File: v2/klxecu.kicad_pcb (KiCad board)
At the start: 4 copper layers, 101.6 x 74.9 mm, 71 parts, among them IC1 SP721, J1 cam_sensor, J2 Conn_01x06, J3 DIP8, J4 Conn_02x04_Counter_Clockwise, J5 TACH_OUT, Q1 SSM3K357R, Q2 SSM3K357R, Q3 STP62NS04Z, Q4 SSM3K357R, Q5 SSM3K357R, Q6 SSM3K357R, Q7 SSM3K357R, U1 S36B-WPZK-A, U2 LM2940S-5.0/NOPB, U3 Arduino Mega 2560 Pro, U4 TC4424AVPA

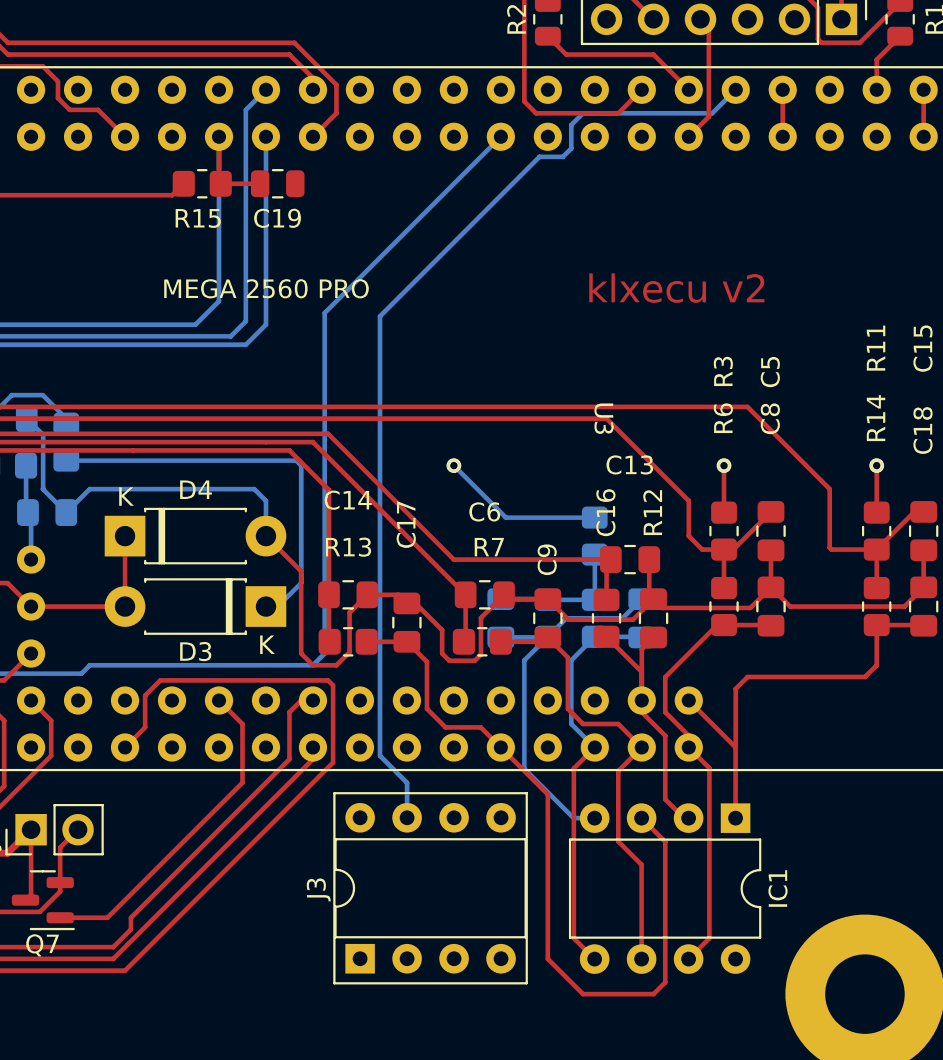
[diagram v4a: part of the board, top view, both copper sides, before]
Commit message: Add reset protection jumper
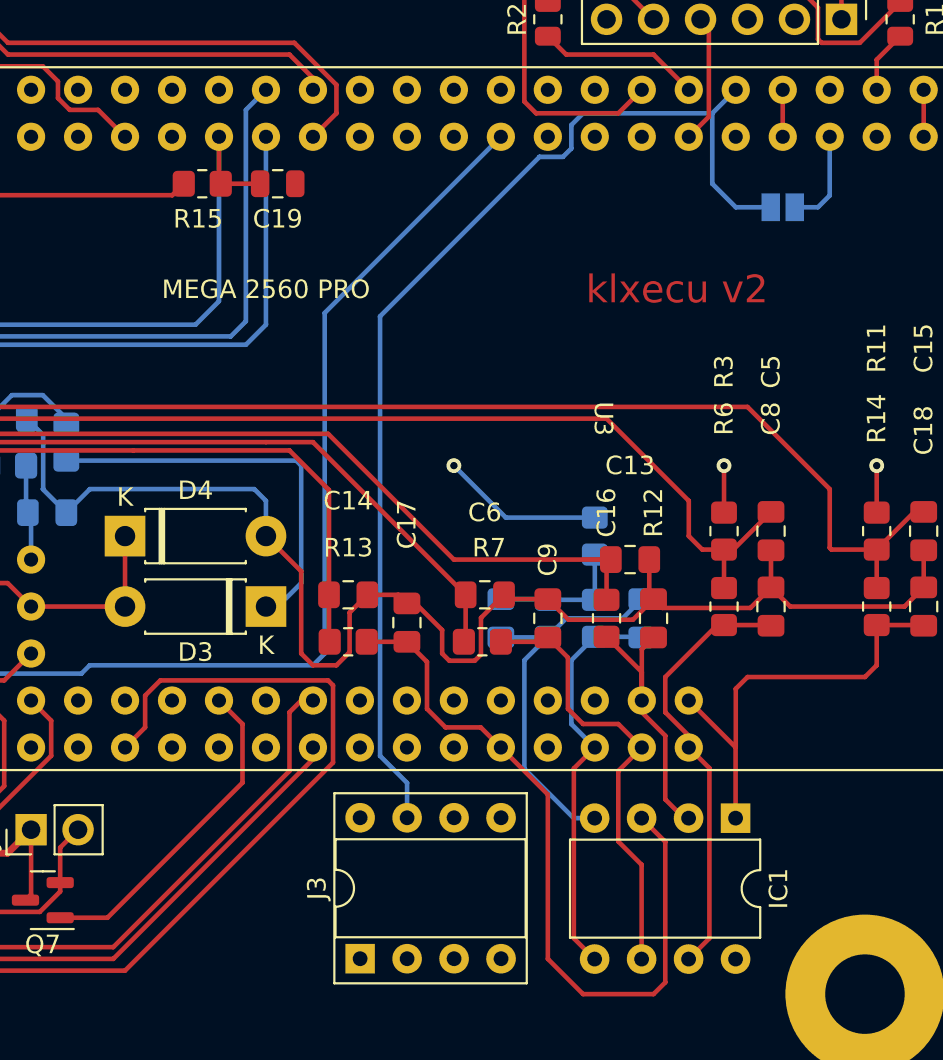
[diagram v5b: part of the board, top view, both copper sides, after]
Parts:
- added JP3: Jumper_2_Open, Jumper:SolderJumper-2_P1.3mm_Open_Pad1.0x1.5mm, B.Cu at (117.5, 66.7)
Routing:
- net ARDUINO-RST: track 52.8 -> 60.3 mm
- net +5V: track 78.0 -> 83.3 mm
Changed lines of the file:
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@@
       (drillshape 0)
       (scaleselection 1)
-      (outputdirectory "gerber/")
+      (outputdirectory "gerber2/")
     )
   )
@@
     (fp_line (start -1 0.625) (end -1 -0.625) (layer "F.Fab") (width 0.1))
     (fp_line (start 1 0.625) (end -1 0.625) (layer "F.Fab") (width 0.1))
-    (pad "1" smd roundrect (at -1.0375 0) (size 1.175 1.45) (layers "F.Cu" "F.Paste" "F.Mask") (roundrect_rratio 0.212766)
+    (pad "1" smd roundrect (at -1.0375 0) (size 1.175 1.45) (layers "F.Cu" "F.Paste" "F.Mask") (roundrect_rratio 0.2127659574)
       (net 119 "O2S") (pintype "passive"))
-    (pad "2" smd roundrect (at 1.0375 0) (size 1.175 1.45) (layers "F.Cu" "F.Paste" "F.Mask") (roundrect_rratio 0.212766)
+    (pad "2" smd roundrect (at 1.0375 0) (size 1.175 1.45) (layers "F.Cu" "F.Paste" "F.Mask") (roundrect_rratio 0.2127659574)
       (net 1 "GND") (pintype "passive"))
     (model "${KICAD6_3DMODEL_DIR}/Capacitor_SMD.3dshapes/C_0805_2012Metric.wrl"
@@
     (fp_line (start -1 0.625) (end -1 -0.625) (layer "F.Fab") (width 0.1))
     (fp_line (start 1 0.625) (end -1 0.625) (layer "F.Fab") (width 0.1))
-    (pad "1" smd roundrect (at -1 0) (size 1.2 1.4) (layers "F.Cu" "F.Paste" "F.Mask") (roundrect_rratio 0.208333)
+    (pad "1" smd roundrect (at -1 0) (size 1.2 1.4) (layers "F.Cu" "F.Paste" "F.Mask") (roundrect_rratio 0.2083333333)
       (net 119 "O2S") (pintype "passive"))
-    (pad "2" smd roundrect (at 1 0) (size 1.2 1.4) (layers "F.Cu" "F.Paste" "F.Mask") (roundrect_rratio 0.208333)
+    (pad "2" smd roundrect (at 1 0) (size 1.2 1.4) (layers "F.Cu" "F.Paste" "F.Mask") (roundrect_rratio 0.2083333333)
       (net 121 "O2S-ARD-A8") (pintype "passive"))
     (model "${KICAD6_3DMODEL_DIR}/Resistor_SMD.3dshapes/R_0805_2012Metric.wrl"
@@
     (fp_line (start -1 -0.625) (end 1 -0.625) (layer "F.Fab") (width 0.1))
     (fp_line (start -1 0.625) (end -1 -0.625) (layer "F.Fab") (width 0.1))
-    (pad "1" smd roundrect (at -1.0375 0 90) (size 1.175 1.45) (layers "F.Cu" "F.Paste" "F.Mask") (roundrect_rratio 0.212766)
+    (pad "1" smd roundrect (at -1.0375 0 90) (size 1.175 1.45) (layers "F.Cu" "F.Paste" "F.Mask") (roundrect_rratio 0.2127659574)
       (net 121 "O2S-ARD-A8") (pintype "passive"))
-    (pad "2" smd roundrect (at 1.0375 0 90) (size 1.175 1.45) (layers "F.Cu" "F.Paste" "F.Mask") (roundrect_rratio 0.212766)
+    (pad "2" smd roundrect (at 1.0375 0 90) (size 1.175 1.45) (layers "F.Cu" "F.Paste" "F.Mask") (roundrect_rratio 0.2127659574)
       (net 1 "GND") (pintype "passive"))
     (model "${KICAD6_3DMODEL_DIR}/Capacitor_SMD.3dshapes/C_0805_2012Metric.wrl"
@@
     )
   )
+  (footprint "Jumper:SolderJumper-2_P1.3mm_Open_Pad1.0x1.5mm" (layer "B.Cu")
+    (at 117.475 66.675 180)
+    (descr "SMD Solder Jumper, 1x1.5mm Pads, 0.3mm gap, open")
+    (tags "solder jumper open")
+    (property "Sheetfile" "sensors.kicad_sch")
+    (property "Sheetname" "Sensors & Inputs")
+    (attr exclude_from_pos_files)
+    (fp_text reference "JP3" (at 0 1.8) (layer "B.SilkS")
+      (effects (font (size 1 1) (thickness 0.15)) (justify mirror))
+    )
+    (fp_text value "Jumper_2_Open" (at 0 -1.9) (layer "B.Fab")
+      (effects (font (size 1 1) (thickness 0.15)) (justify mirror))
+    )
+    (fp_line (start 1.4 1) (end 1.4 -1) (layer "B.SilkS") (width 0.12))
+    (fp_line (start 1.4 -1) (end -1.4 -1) (layer "B.SilkS") (width 0.12))
+    (fp_line (start -1.4 1) (end 1.4 1) (layer "B.SilkS") (width 0.12))
+    (fp_line (start -1.4 -1) (end -1.4 1) (layer "B.SilkS") (width 0.12))
+    (fp_line (start 1.65 -1.25) (end 1.65 1.25) (layer "B.CrtYd") (width 0.05))
+    (fp_line (start -1.65 1.25) (end -1.65 -1.25) (layer "B.CrtYd") (width 0.05))
+    (fp_line (start -1.65 1.25) (end 1.65 1.25) (layer "B.CrtYd") (width 0.05))
+    (fp_line (start 1.65 -1.25) (end -1.65 -1.25) (layer "B.CrtYd") (width 0.05))
+    (pad "1" smd rect (at -0.65 0 180) (size 1 1.5) (layers "B.Cu" "B.Mask")
+      (net 2 "+5V") (pinfunction "A") (pintype "passive"))
+    (pad "2" smd rect (at 0.65 0 180) (size 1 1.5) (layers "B.Cu" "B.Mask")
+      (net 104 "ARDUINO-RST") (pinfunction "B") (pintype "passive"))
+  )
   (footprint "Resistor_SMD:R_0805_2012Metric_Pad1.20x1.40mm_HandSolder" (layer "B.Cu")
     (at 78.74 79.375 90)
@@
   (via (at 114.3 80.645) (size 0.8) (drill 0.4) (layers "F.Cu" "B.Cu") (net 2))
   (via (at 74.93 52.705) (size 0.8) (drill 0.4) (layers "F.Cu" "B.Cu") (free) (net 2))
+  (segment (start 119.38 66.675) (end 118.125 66.675) (width 0.25) (layer "B.Cu") (net 2))
   (segment (start 91.17 80.375) (end 91.44 80.645) (width 0.25) (layer "B.Cu") (net 2))
   (segment (start 46.355 101.8325) (end 46.345 101.8425) (width 1) (layer "B.Cu") (net 2))
+  (segment (start 120.015 62.865) (end 120.015 66.04) (width 0.25) (layer "B.Cu") (net 2))
   (segment (start 90.17 88.265) (end 89.535 88.265) (width 0.25) (layer "B.Cu") (net 2))
   (segment (start 91.44 86.995) (end 90.17 88.265) (width 0.25) (layer "B.Cu") (net 2))
@@
   (segment (start 78.74 80.375) (end 91.17 80.375) (width 0.25) (layer "B.Cu") (net 2))
   (segment (start 91.44 80.645) (end 91.44 86.995) (width 0.25) (layer "B.Cu") (net 2))
+  (segment (start 120.015 66.04) (end 119.38 66.675) (width 0.25) (layer "B.Cu") (net 2))
   (segment (start 62.059511 63.945433) (end 61.415433 64.589511) (width 0.2) (layer "B.Cu") (net 3))
   (segment (start 31.169511 59.259828) (end 32.408859 58.02048) (width 0.2) (layer "B.Cu") (net 3))
@@
   (segment (start 28.845489 91.574511) (end 30.02 90.4) (width 0.25) (layer "In2.Cu") (net 38))
   (segment (start 29.533501 96.574511) (end 28.845489 95.886499) (width 0.25) (layer "In2.Cu") (net 38))
+  (segment (start 81.279282 106.68) (end 90.805 97.154282) (width 0.25) (layer "F.Cu") (net 39))
+  (segment (start 90.805 93.98) (end 91.44 93.345) (width 0.25) (layer "F.Cu") (net 39))
+  (segment (start 90.805 97.154282) (end 90.805 93.98) (width 0.25) (layer "F.Cu") (net 39))
+  (segment (start 91.44 93.345) (end 92.075 93.345) (width 0.25) (layer "F.Cu") (net 39))
   (segment (start 72.0575 105.09) (end 73.6475 106.68) (width 0.25) (layer "F.Cu") (net 39))
-  (segment (start 82.235 105.09) (end 90.805 96.52) (width 0.25) (layer "F.Cu") (net 39))
-  (segment (start 90.805 96.52) (end 90.805 93.98) (width 0.25) (layer "F.Cu") (net 39))
-  (segment (start 81.279282 106.68) (end 82.235 105.724282) (width 0.25) (layer "F.Cu") (net 39))
-  (segment (start 82.235 105.724282) (end 82.235 105.09) (width 0.25) (layer "F.Cu") (net 39))
   (segment (start 73.6475 106.68) (end 81.279282 106.68) (width 0.25) (layer "F.Cu") (net 39))
-  (segment (start 91.44 93.345) (end 92.075 93.345) (width 0.25) (layer "F.Cu") (net 39))
-  (segment (start 90.805 93.98) (end 91.44 93.345) (width 0.25) (layer "F.Cu") (net 39))
   (segment (start 68.58 104.14) (end 70.1825 104.14) (width 0.25) (layer "F.Cu") (net 40))
   (via (at 68.58 104.14) (size 0.8) (drill 0.4) (layers "F.Cu" "B.Cu") (net 40))
@@
   (segment (start 106.045 62.23) (end 106.68 61.595) (width 0.25) (layer "B.Cu") (net 104))
   (segment (start 106.68 61.595) (end 113.665 61.595) (width 0.25) (layer "B.Cu") (net 104))
+  (segment (start 113.665 65.405) (end 114.935 66.675) (width 0.25) (layer "B.Cu") (net 104))
   (segment (start 97.165 99.685) (end 97.165 97.8) (width 0.25) (layer "B.Cu") (net 104))
   (segment (start 95.701511 96.336511) (end 95.701511 72.574207) (width 0.25) (layer "B.Cu") (net 104))
+  (segment (start 114.935 66.675) (end 116.825 66.675) (width 0.25) (layer "B.Cu") (net 104))
+  (segment (start 113.665 61.595) (end 113.665 65.405) (width 0.25) (layer "B.Cu") (net 104))
   (segment (start 104.324579 63.951139) (end 104.324951 63.951511) (width 0.25) (layer "B.Cu") (net 104))
   (segment (start 104.324951 63.951511) (end 105.593489 63.951511) (width 0.25) (layer "B.Cu") (net 104))
